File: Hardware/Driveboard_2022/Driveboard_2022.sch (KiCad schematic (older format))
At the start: 95 parts, among them SW1 SW_SPST, SW2 SW_SPST, SW3 SW_SPST, SW4 SW_SPST, SW5 SW_SPST, SW6 SW_SPST, SW7 SW_SPST, U1 TM4C129E_Launchpad, U2 MAX_3232, U3 MAX_3232, U4 MAX_3232, U5 OKI 3V3, U6 OKI 5V

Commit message: Changed Switches Back to Buttons; Created Schematic PDF
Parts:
- removed SW1, SW2, SW3, SW5, SW6, SW7: SW_SPST, symbol Switch:SW_SPST
- added SW1, SW2, SW3, SW5, SW6, SW7: SW_Push, symbol Switch:SW_Push
- Conn13: symbol Driveboard_2022-rescue:AndersonPP-MRDT_Connectors -> Driveboard_2022-rescue:AndersonPP-MRDT_Connectors-Driveboard_2022-rescue
- U2, U3, U4: symbol Driveboard_2022-rescue:MAX_3232-MRDT_ICs -> Driveboard_2022-rescue:MAX_3232-MRDT_ICs-Driveboard_2022-rescue
- U5, U6: symbol Driveboard_2022-rescue:OKI-MRDT_Devices -> Driveboard_2022-rescue:OKI-MRDT_Devices-Driveboard_2022-rescue
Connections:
- net +3V3: now also SW1.1, SW2.1, SW3.1, SW5.1, SW6.1, SW7.1
- net BL_DRIVE: now also SW3.2
- net BR_DRIVE: now also SW7.2
- net FL_DRIVE: now also SW1.2
- net FR_DRIVE: now also SW5.2
- net ML_DRIVE: now also SW2.2
- net MR_DRIVE: now also SW6.2
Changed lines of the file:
@@
 $EndComp
 $Comp
-L Driveboard_2022-rescue:AndersonPP-MRDT_Connectors Conn13
+L Driveboard_2022-rescue:AndersonPP-MRDT_Connectors-Driveboard_2022-rescue Conn13
 U 2 1 614AE409
 P 10400 1000
@@
 $EndComp
 $Comp
-L Driveboard_2022-rescue:OKI-MRDT_Devices U5
+L Driveboard_2022-rescue:OKI-MRDT_Devices-Driveboard_2022-rescue U5
 U 1 1 614A9918
 P 900 1150
@@
 $EndComp
 $Comp
-L Driveboard_2022-rescue:AndersonPP-MRDT_Connectors Conn13
+L Driveboard_2022-rescue:AndersonPP-MRDT_Connectors-Driveboard_2022-rescue Conn13
 U 1 1 614B9C60
 P 10400 1300
@@
 $EndComp
 $Comp
-L Driveboard_2022-rescue:MAX_3232-MRDT_ICs U2
+L Driveboard_2022-rescue:MAX_3232-MRDT_ICs-Driveboard_2022-rescue U2
 U 1 1 617D8921
 P 1450 3450
@@
 	2350 2900 2900 2900
 $Comp
-L Driveboard_2022-rescue:MAX_3232-MRDT_ICs U3
+L Driveboard_2022-rescue:MAX_3232-MRDT_ICs-Driveboard_2022-rescue U3
 U 1 1 61A97194
 P 1450 4900
@@
 	2350 4350 2900 4350
 $Comp
-L Driveboard_2022-rescue:MAX_3232-MRDT_ICs U4
+L Driveboard_2022-rescue:MAX_3232-MRDT_ICs-Driveboard_2022-rescue U4
 U 1 1 61AC0352
 P 1450 6350
@@
 $EndComp
 $Comp
-L Driveboard_2022-rescue:OKI-MRDT_Devices U6
+L Driveboard_2022-rescue:OKI-MRDT_Devices-Driveboard_2022-rescue U6
 U 1 1 61EEB36B
 P 2250 1150
@@
 	9600 5950 9600 6100
 $Comp
-L Switch:SW_SPST SW3
-U 1 1 616C949B
+L Switch:SW_Push SW1
+U 1 1 61746F56
+P 4250 4200
+F 0 "SW1" H 4250 4485 50  0000 C CNN
+F 1 "SW_Push" H 4250 4394 50  0000 C CNN
+F 2 "" H 4250 4400 50  0001 C CNN
+F 3 "~" H 4250 4400 50  0001 C CNN
+	1    4250 4200
+	1    0    0    -1
+$EndComp
+$Comp
+L Switch:SW_Push SW2
+U 1 1 617B9ED6
+P 4250 4700
+F 0 "SW2" H 4250 4985 50  0000 C CNN
+F 1 "SW_Push" H 4250 4894 50  0000 C CNN
+F 2 "" H 4250 4900 50  0001 C CNN
+F 3 "~" H 4250 4900 50  0001 C CNN
+	1    4250 4700
+	1    0    0    -1
+$EndComp
+$Comp
+L Switch:SW_Push SW3
+U 1 1 617E000A
 P 4250 5200
-F 0 "SW3" H 4250 5435 50  0000 C CNN
-F 1 "SW_SPST" H 4250 5344 50  0000 C CNN
-F 2 "" H 4250 5200 50  0001 C CNN
-F 3 "~" H 4250 5200 50  0001 C CNN
+F 0 "SW3" H 4250 5485 50  0000 C CNN
+F 1 "SW_Push" H 4250 5394 50  0000 C CNN
+F 2 "" H 4250 5400 50  0001 C CNN
+F 3 "~" H 4250 5400 50  0001 C CNN
 	1    4250 5200
 	1    0    0    -1
 $EndComp
 $Comp
-L Switch:SW_SPST SW2
-U 1 1 616EF582
-P 4250 4700
-F 0 "SW2" H 4250 4935 50  0000 C CNN
-F 1 "SW_SPST" H 4250 4844 50  0000 C CNN
-F 2 "" H 4250 4700 50  0001 C CNN
-F 3 "~" H 4250 4700 50  0001 C CNN
-	1    4250 4700
-	1    0    0    -1
-$EndComp
-$Comp
-L Switch:SW_SPST SW1
-U 1 1 61715659
-P 4250 4200
-F 0 "SW1" H 4250 4435 50  0000 C CNN
-F 1 "SW_SPST" H 4250 4344 50  0000 C CNN
-F 2 "" H 4250 4200 50  0001 C CNN
-F 3 "~" H 4250 4200 50  0001 C CNN
-	1    4250 4200
-	1    0    0    -1
-$EndComp
-$Comp
-L Switch:SW_SPST SW5
-U 1 1 6173B76C
+L Switch:SW_Push SW5
+U 1 1 618062D7
 P 6000 4200
-F 0 "SW5" H 6000 4435 50  0000 C CNN
-F 1 "SW_SPST" H 6000 4344 50  0000 C CNN
-F 2 "" H 6000 4200 50  0001 C CNN
-F 3 "~" H 6000 4200 50  0001 C CNN
+F 0 "SW5" H 6000 4485 50  0000 C CNN
+F 1 "SW_Push" H 6000 4394 50  0000 C CNN
+F 2 "" H 6000 4400 50  0001 C CNN
+F 3 "~" H 6000 4400 50  0001 C CNN
 	1    6000 4200
 	1    0    0    -1
 $EndComp
 $Comp
-L Switch:SW_SPST SW6
-U 1 1 617618B1
+L Switch:SW_Push SW6
+U 1 1 6182C518
 P 6000 4700
-F 0 "SW6" H 6000 4935 50  0000 C CNN
-F 1 "SW_SPST" H 6000 4844 50  0000 C CNN
-F 2 "" H 6000 4700 50  0001 C CNN
-F 3 "~" H 6000 4700 50  0001 C CNN
+F 0 "SW6" H 6000 4985 50  0000 C CNN
+F 1 "SW_Push" H 6000 4894 50  0000 C CNN
+F 2 "" H 6000 4900 50  0001 C CNN
+F 3 "~" H 6000 4900 50  0001 C CNN
 	1    6000 4700
 	1    0    0    -1
 $EndComp
 $Comp
-L Switch:SW_SPST SW7
-U 1 1 617878FC
+L Switch:SW_Push SW7
+U 1 1 6185281C
 P 6000 5200
-F 0 "SW7" H 6000 5435 50  0000 C CNN
-F 1 "SW_SPST" H 6000 5344 50  0000 C CNN
-F 2 "" H 6000 5200 50  0001 C CNN
-F 3 "~" H 6000 5200 50  0001 C CNN
+F 0 "SW7" H 6000 5485 50  0000 C CNN
+F 1 "SW_Push" H 6000 5394 50  0000 C CNN
+F 2 "" H 6000 5400 50  0001 C CNN
+F 3 "~" H 6000 5400 50  0001 C CNN
 	1    6000 5200
 	1    0    0    -1

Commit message: 6-Pin Molex and Layour from B
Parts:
- removed Conn1, Conn10, Conn11, Conn12, Conn2, Conn3, Conn4, Conn5, Conn6, Conn7, Conn8, Conn9: Molex_uF_S_03, MRDT_Connectors:MOLEX_uF_S_03_Horizontal, symbol MRDT_Connectors:Molex_uF_S_03
- added Conn1, Conn2, Conn3, Conn4, Conn5, Conn6: Molex_uF_D_06, MRDT_Connectors:MOLEX_uF_D_06_Horizontal, symbol MRDT_Connectors:Molex_uF_D_06
- C1, C10, C11, C12, C13, C2, C3, C4, C5, C6, C7, C8, C9: footprint (none) -> Capacitor_SMD:C_0603_1608Metric_Pad1.08x0.95mm_HandSolder
- Conn13: footprint (none) -> MRDT_Connectors:Anderson_2_Horizontal_Side_by_Side; symbol Driveboard_2022-rescue:AndersonPP-MRDT_Connectors-Driveboard_2022-rescue -> Driveboard_2022-rescue:AndersonPP-MRDT_Connectors-Driveboard_2022-rescue-Driveboard_2022-rescue
- LED1, LED10, LED11, LED12, LED13, LED14, LED15, LED16, LED17, LED18, LED19, LED2, LED20, LED21, LED22, LED23, LED24, LED25, LED26, LED27, LED28, LED3, LED4, LED5, LED6, LED7, LED8, LED9: footprint (none) -> LED_SMD:LED_0603_1608Metric_Pad1.05x0.95mm_HandSolder
- R1, R10, R11, R12, R13, R14, R15, R16, R17, R18, R19, R2, R20, R21, R22, R23, R24, R25, R26, R27, R28, R3, R4, R5, R6, R7, R8, R9: footprint (none) -> Resistor_SMD:R_0603_1608Metric_Pad0.98x0.95mm_HandSolder
- SW1, SW2, SW3, SW5, SW6, SW7: footprint (none) -> Button_Switch_SMD:SW_Push_1P1T_NO_6x6mm_H9.5mm
- SW4: footprint (none) -> MRDT_Switches:1P2T_Angled_Slide_GPI-152-3013
- U1: footprint (none) -> MRDT_Shields:TM4C129E_Launchpad_FULL_Vertical
- U2, U3, U4: footprint (none) -> Package_SO:SOIC-16_3.9x9.9mm_P1.27mm; symbol Driveboard_2022-rescue:MAX_3232-MRDT_ICs-Driveboard_2022-rescue -> Driveboard_2022-rescue:MAX_3232-MRDT_ICs-Driveboard_2022-rescue-Driveboard_2022-rescue
- U5, U6: footprint (none) -> MRDT_Devices:OKI_Horizontal; symbol Driveboard_2022-rescue:OKI-MRDT_Devices-Driveboard_2022-rescue -> Driveboard_2022-rescue:OKI-MRDT_Devices-Driveboard_2022-rescue-Driveboard_2022-rescue
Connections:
- net BLRX: now also Conn5.3
- net BLRX_V: now also Conn5.6; no longer R25.1, U1.PA4 (B2_9), U4.12 (Rx1_OUT)
- net BLTX: now also Conn5.1
- net BLTX_V: now also Conn5.4; no longer R26.1, U1.PA5 (B2_10), U4.11 (Tx1_IN)
- net BRRX: now also Conn6.3
- net BRRX_V: now also Conn6.6; no longer R27.1, U1.PA6 (B1_8), U4.9 (Rx2OUT)
- net BRTX: now also Conn6.1
- net BRTX_V: now also Conn6.4; no longer R28.1, U1.PA7 (D2_4), U4.10 (Tx2_IN)
- net FLRX: now also Conn1.3
- net FLRX_V: now also Conn1.6
- net FLTX: now also Conn1.1
- net FLTX_V: now also Conn1.4
- net FRRX: now also Conn2.3
- net FRRX_V: now also Conn2.6
- net FRTX: now also Conn2.1
- net FRTX_V: now also Conn2.4
- net GND: now also Conn1.2, Conn1.5, Conn2.2, Conn2.5, Conn3.2, Conn3.5, Conn4.2, Conn4.5, Conn5.2, Conn5.5, Conn6.2, Conn6.5
- net MLRX: now also Conn3.3
- net MLRX_V: now also R25.1, U1.PA4 (B2_9), U4.12 (Rx1_OUT), Conn3.6
- net MLTX: now also Conn3.1
- net MLTX_V: now also R26.1, U1.PA5 (B2_10), U4.11 (Tx1_IN), Conn3.4
- net MRRX: now also Conn4.3
- net MRRX_V: now also R27.1, U4.9 (Rx2OUT), Conn4.6
- net MRTX: now also Conn4.1
- net MRTX_V: now also R28.1, U1.PA7 (D2_4), U4.10 (Tx2_IN), Conn4.4
- new net RX2: U1.PA6 (B1_8)

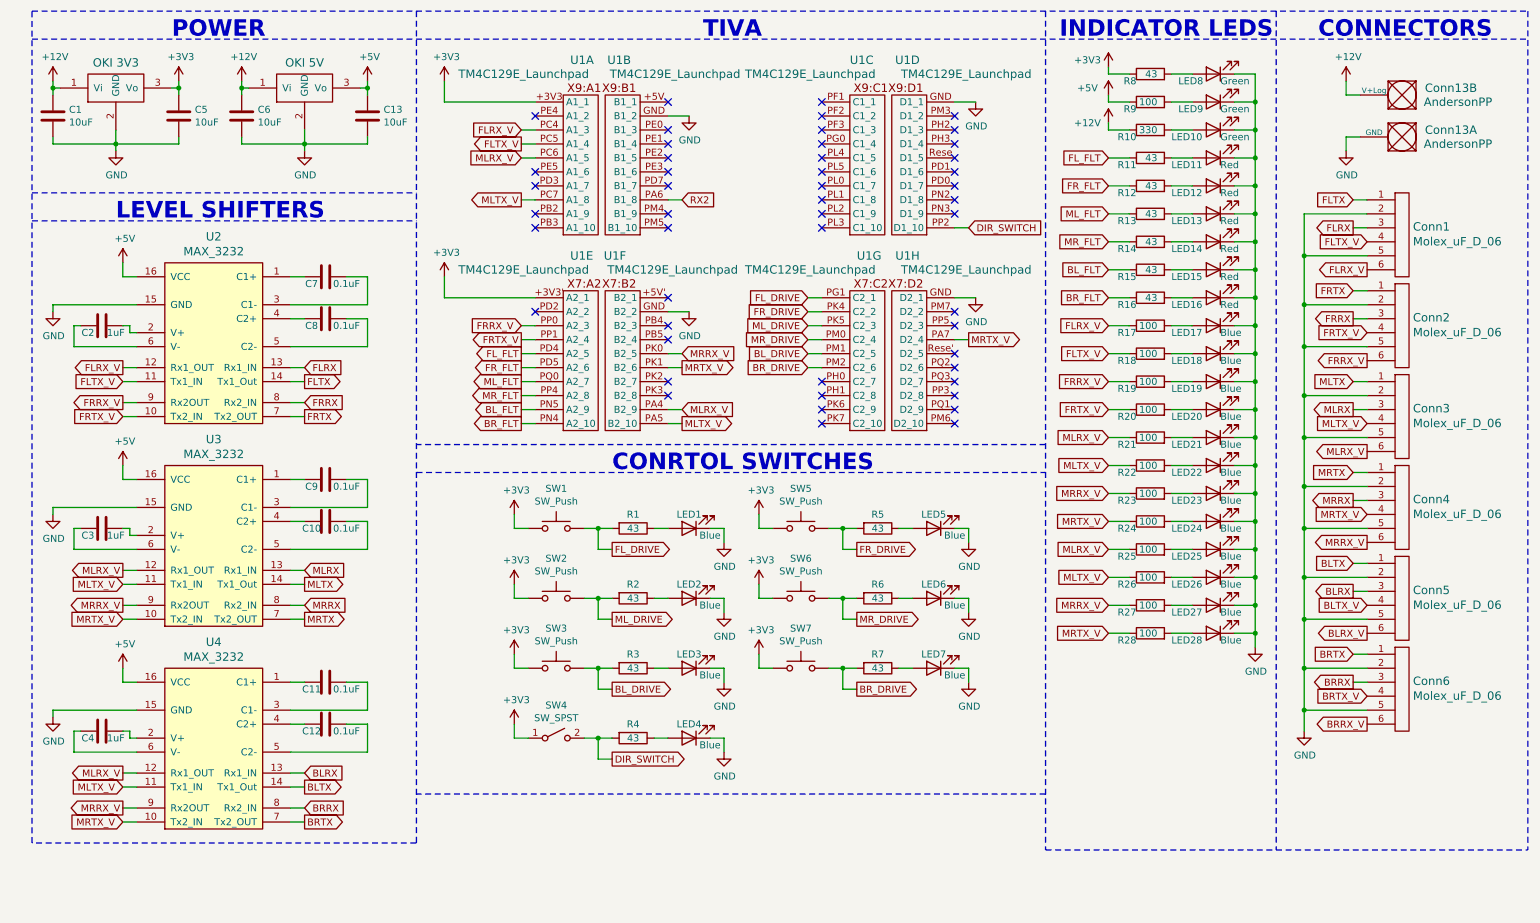
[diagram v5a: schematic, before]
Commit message: Fix Mislabeled Serial Connections, Serial Traces, GND Vias
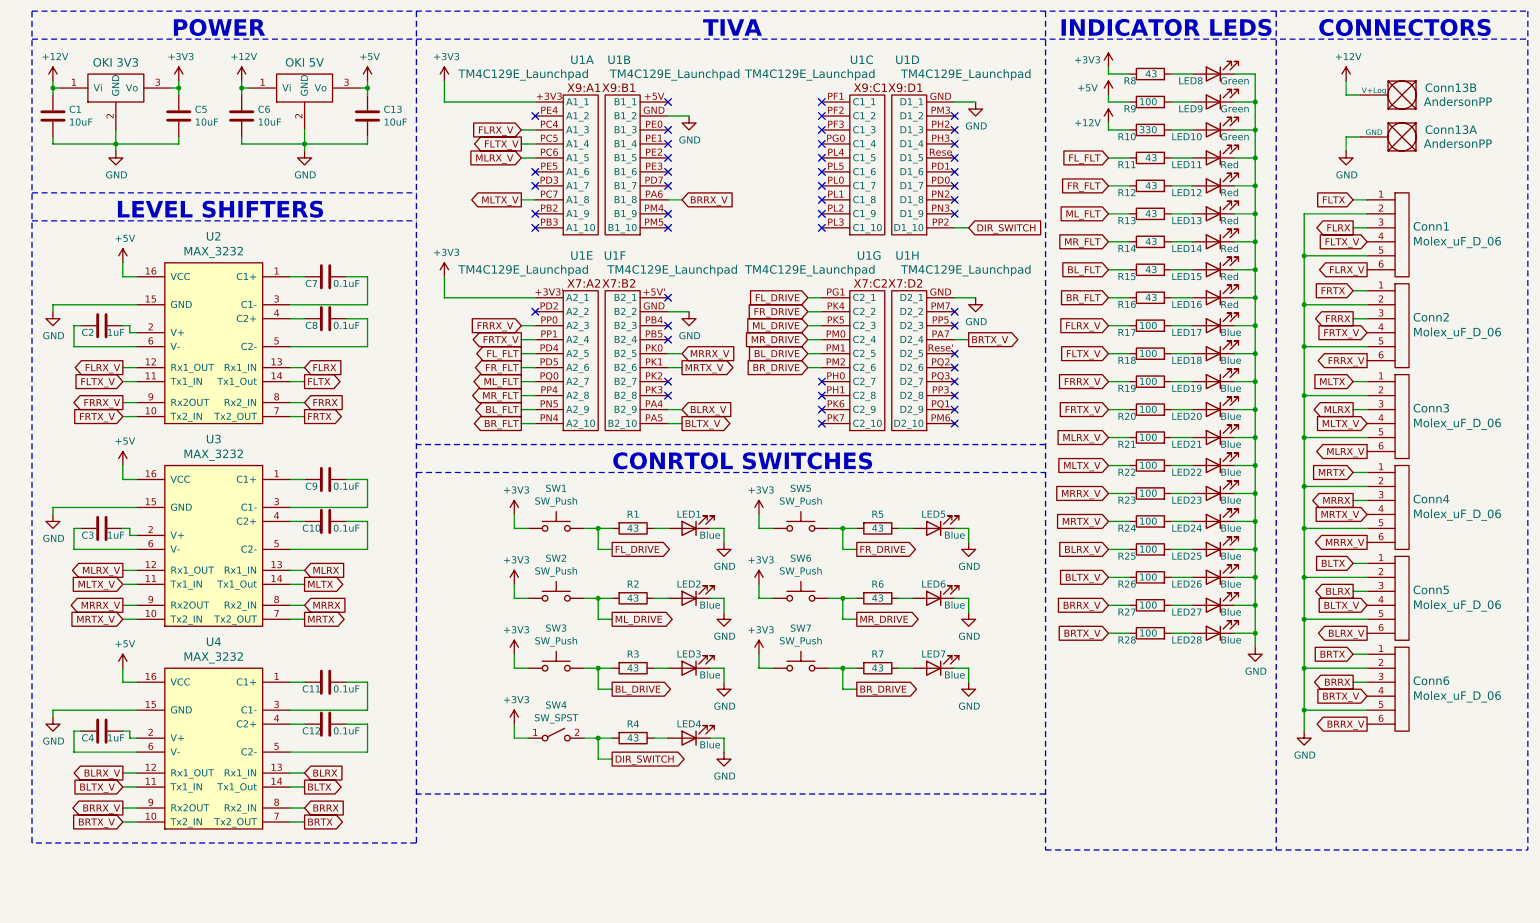
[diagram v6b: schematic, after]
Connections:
- net RX2 is gone; now on net BRRX_V: U1.PA6 (B1_8)
- net BLRX_V: now also R25.1, U1.PA4 (B2_9), U4.12 (Rx1_OUT)
- net BLTX_V: now also R26.1, U1.PA5 (B2_10), U4.11 (Tx1_IN)
- net BRRX_V: now also R27.1, U4.9 (Rx2OUT)
- net BRTX_V: now also R28.1, U1.PA7 (D2_4), U4.10 (Tx2_IN)
- net MLRX_V: no longer R25.1, U1.PA4 (B2_9), U4.12 (Rx1_OUT)
- net MLTX_V: no longer R26.1, U1.PA5 (B2_10), U4.11 (Tx1_IN)
- net MRRX_V: no longer R27.1, U4.9 (Rx2OUT)
- net MRTX_V: no longer R28.1, U1.PA7 (D2_4), U4.10 (Tx2_IN)
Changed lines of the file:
@@
 	4000 1850 4100 1850
 Text GLabel 5150 1850 2    50   Input ~ 0
-RX2
+BRRX_V
 Wire Wire Line
 	5150 1850 5050 1850
 Text GLabel 7200 2850 2    50   Output ~ 0
-MRTX_V
+BRTX_V
 Wire Wire Line
 	7200 2850 7100 2850
@@
 FRTX_V
 Text GLabel 8200 4550 0    50   Input ~ 0
-MLTX_V
+BLTX_V
 $Comp
 L Device:R R19
@@
 FRRX_V
 Text GLabel 8200 4350 0    50   Input ~ 0
-MLRX_V
+BLRX_V
 $Comp
 L Device:R R17
@@
 $EndComp
 Text GLabel 8200 4750 0    50   Input ~ 0
-MRRX_V
+BRRX_V
 Text GLabel 8200 3550 0    50   Input ~ 0
 MLRX_V
@@
 $EndComp
 Text GLabel 8200 4950 0    50   Input ~ 0
-MRTX_V
+BRTX_V
 Text GLabel 8200 3750 0    50   Input ~ 0
 MLTX_V
@@
 BLTX
 Text GLabel 1150 5950 0    50   Output ~ 0
-MLRX_V
+BLRX_V
 Text GLabel 1150 6050 0    50   Input ~ 0
-MLTX_V
+BLTX_V
 Text GLabel 1150 6200 0    50   Output ~ 0
-MRRX_V
+BRRX_V
 Text GLabel 1150 6300 0    50   Input ~ 0
-MRTX_V
+BRTX_V
 Wire Wire Line
 	2450 6050 2350 6050
@@
 	5150 3350 5050 3350
 Text GLabel 5150 3450 2    50   Output ~ 0
-MLTX_V
+BLTX_V
 Text GLabel 5150 3350 2    50   Input ~ 0
-MLRX_V
+BLRX_V
 Wire Wire Line
 	5150 3050 5050 3050

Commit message: Removed rescue library for symbols
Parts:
- Conn13: symbol Driveboard_2022-rescue:AndersonPP-MRDT_Connectors-Driveboard_2022-rescue-Driveboard_2022-rescue -> MRDT_Connectors:AndersonPP
- U2, U3, U4: symbol Driveboard_2022-rescue:MAX_3232-MRDT_ICs-Driveboard_2022-rescue-Driveboard_2022-rescue -> MRDT_ICs:MAX_3232
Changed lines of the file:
@@
 $EndComp
 $Comp
-L Driveboard_2022-rescue:AndersonPP-MRDT_Connectors-Driveboard_2022-rescue-Driveboard_2022-rescue Conn13
+L MRDT_Connectors:AndersonPP Conn13
 U 2 1 614AE409
 P 10400 1000
@@
 $EndComp
 $Comp
-L Driveboard_2022-rescue:AndersonPP-MRDT_Connectors-Driveboard_2022-rescue-Driveboard_2022-rescue Conn13
+L MRDT_Connectors:AndersonPP Conn13
 U 1 1 614B9C60
 P 10400 1300
@@
 $EndComp
 $Comp
-L Driveboard_2022-rescue:MAX_3232-MRDT_ICs-Driveboard_2022-rescue-Driveboard_2022-rescue U2
+L MRDT_ICs:MAX_3232 U2
 U 1 1 617D8921
 P 1450 3450
@@
 	2350 2900 2900 2900
 $Comp
-L Driveboard_2022-rescue:MAX_3232-MRDT_ICs-Driveboard_2022-rescue-Driveboard_2022-rescue U3
+L MRDT_ICs:MAX_3232 U3
 U 1 1 61A97194
 P 1450 4900
@@
 	2350 4350 2900 4350
 $Comp
-L Driveboard_2022-rescue:MAX_3232-MRDT_ICs-Driveboard_2022-rescue-Driveboard_2022-rescue U4
+L MRDT_ICs:MAX_3232 U4
 U 1 1 61AC0352
 P 1450 6350

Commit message: Finished Schematic and Layout
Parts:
- removed C10, C11, C12, C7, C8, C9: 0.1uF, Capacitor_SMD:C_0603_1608Metric_Pad1.08x0.95mm_HandSolder, symbol Device:C
- removed C13, C6: 10uF, Capacitor_SMD:C_0603_1608Metric_Pad1.08x0.95mm_HandSolder, symbol Device:C
- removed C2, C3, C4: 1uF, Capacitor_SMD:C_0603_1608Metric_Pad1.08x0.95mm_HandSolder, symbol Device:C
- removed Conn1, Conn2, Conn3, Conn4, Conn5, Conn6: Molex_uF_D_06, MRDT_Connectors:MOLEX_uF_D_06_Horizontal, symbol MRDT_Connectors:Molex_uF_D_06
- removed LED11, LED12, LED13, LED14, LED15, LED16: Red, LED_SMD:LED_0603_1608Metric_Pad1.05x0.95mm_HandSolder, symbol Device:LED
- removed LED9: Green, LED_SMD:LED_0603_1608Metric_Pad1.05x0.95mm_HandSolder, symbol Device:LED
- removed R11, R12, R13, R14, R15, R16: 43, Resistor_SMD:R_0603_1608Metric_Pad0.98x0.95mm_HandSolder, symbol Device:R
- removed R9: 100, Resistor_SMD:R_0603_1608Metric_Pad0.98x0.95mm_HandSolder, symbol Device:R
- removed U1: TM4C129E_Launchpad, MRDT_Shields:TM4C129E_Launchpad_FULL_Vertical, symbol MRDT_Shields:TM4C129E_Launchpad
- removed U2, U3, U4: MAX_3232, Package_SO:SOIC-16_3.9x9.9mm_P1.27mm, symbol MRDT_ICs:MAX_3232
- removed U5: OKI 3V3, MRDT_Devices:OKI_Horizontal, symbol Driveboard_2022-rescue:OKI-MRDT_Devices-Driveboard_2022-rescue-Driveboard_2022-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
- removed U6: OKI 5V, MRDT_Devices:OKI_Horizontal, symbol Driveboard_2022-rescue:OKI-MRDT_Devices-Driveboard_2022-rescue-Driveboard_2022-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
- added Conn1, Conn2, Conn3, Conn4, Conn5, Conn6: Molex_uF_S_03, MRDT_Connectors:MOLEX_uF_S_03_Horizontal, symbol MRDT_Connectors:Molex_uF_S_03
- added U1: OKI 3V3, MRDT_Devices:OKI_Horizontal, symbol MRDT_Devices:OKI
- added U2: Teensy4.1_DEV-16771, MRDT_Shields:Teensy_4_1_Vertical, symbol MRDT_Shields:Teensy4.1_DEV-16771
- SW1, SW2, SW3, SW5, SW6, SW7: footprint Button_Switch_SMD:SW_Push_1P1T_NO_6x6mm_H9.5mm -> Button_Switch_SMD:SW_SPST_TL3305A
- SW4: footprint MRDT_Switches:1P2T_Angled_Slide_GPI-152-3013 -> Button_Switch_THT:SW_Slide_1P2T_CK_OS102011MS2Q
- renumbered LED17 to LED10, LED18 to LED11, LED19 to LED12, LED20 to LED13, LED21 to LED14, LED22 to LED15, LED23 to LED16, LED24 to LED17, LED25 to LED18, LED26 to LED19, LED27 to LED20, LED28 to LED21, LED10 to LED9, R17 to R10, R18 to R11, R19 to R12, R20 to R13, R21 to R14, R22 to R15, R23 to R16, R24 to R17, R25 to R18, R26 to R19, R27 to R20, R28 to R21, R10 to R9
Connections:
- net labels removed: +5V, BLRX_V, BLTX_V, BL_FLT, BRRX_V, BRTX_V, BR_FLT, FLRX_V, FLTX_V, FL_FLT, FRRX_V, FRTX_V, FR_FLT, MLRX_V, MLTX_V, ML_FLT, MRRX_V, MRTX_V, MR_FLT
- wire segments 325 -> 184
- no-connect marks 49 -> 36
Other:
- note added: "TEENSY"
- note removed: "LEVEL SHIFTERS"
- note removed: "TIVA"
- moved on the sheet: C1, C5, LED1, LED10, LED11, LED12, LED13, LED14, LED15, LED16, LED17, LED18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
